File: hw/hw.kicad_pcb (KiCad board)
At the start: 2 copper layers, 120 x 50 mm, 91 parts, among them J1 USB_C_Receptacle, J10 Conn_01x04_Male, J11 Conn_01x04_Male, J12 Conn_01x04_Male, J13 Conn_01x04_Male, J14 Conn_01x04_Male, J16 Conn_01x02_Female, J17 Conn_01x02_Female, J18 Conn_01x04_Female, J19 Conn_01x08_Male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

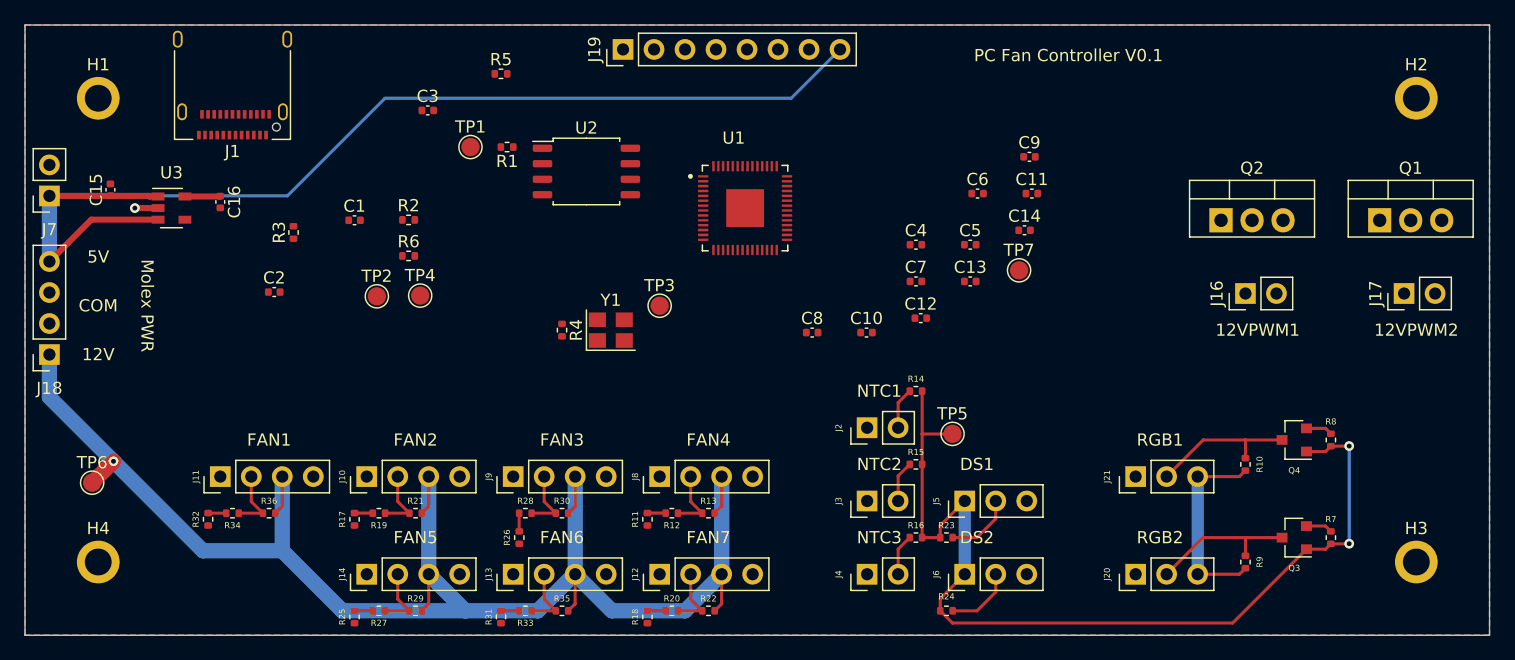
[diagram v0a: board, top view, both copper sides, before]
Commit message: rooting progress + update readme + change power transistor
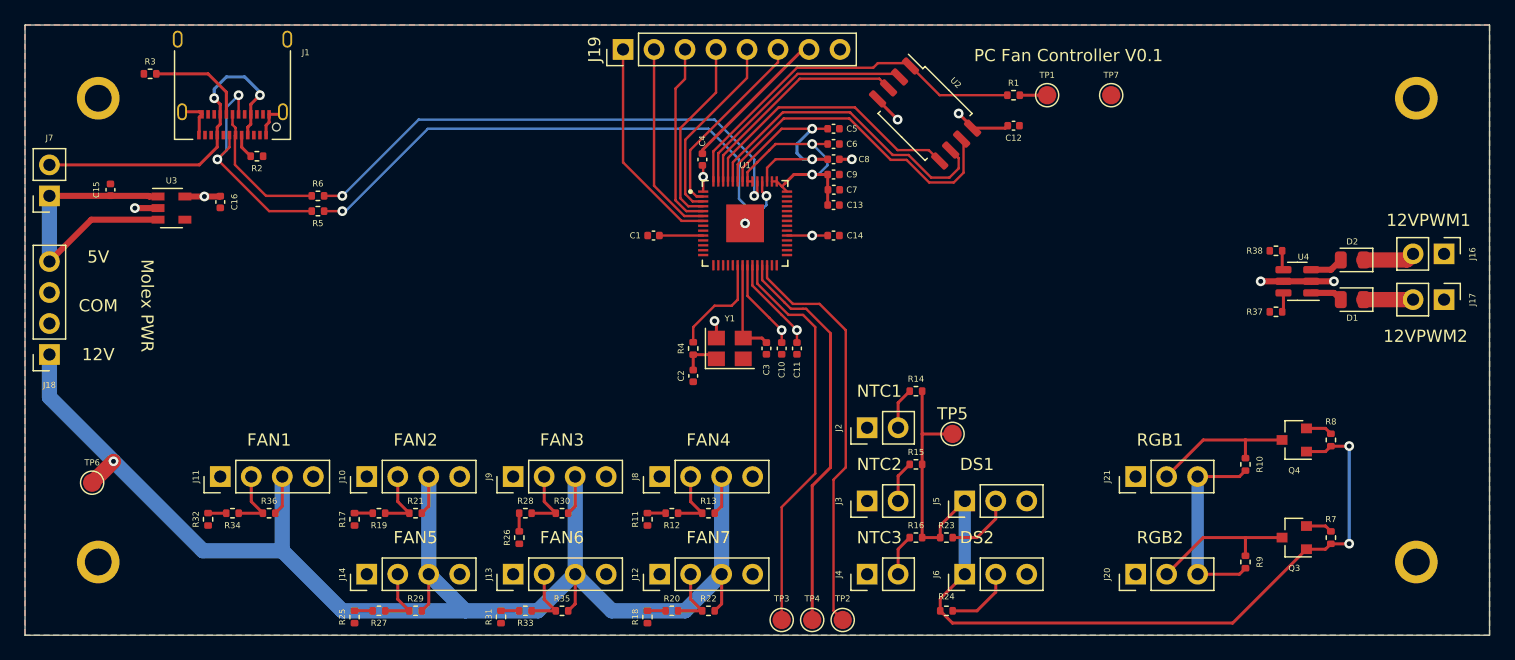
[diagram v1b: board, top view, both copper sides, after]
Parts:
- removed Q1, Q2: IRF540N, Package_TO_SOT_THT:TO-220-3_Vertical
- added D1: D, Diode_SMD:D_0805_2012Metric, F.Cu at (188.8, 42.5)
- added D2: D, Diode_SMD:D_0805_2012Metric, F.Cu at (188.8, 39.2)
- added R37: 10K, Resistor_SMD:R_0402_1005Metric, F.Cu at (182.5, 43.5)
- added R38: 10K, Resistor_SMD:R_0402_1005Metric, F.Cu at (182.5, 38.5)
- added U4: TPM8205ATS6, Package_TO_SOT_SMD:TSOT-23-6, F.Cu at (184.2, 41.0)
- moved TP1 47.4 mm to (163.8, 25.8)
- moved TP2 46.5 mm to (147.0, 68.8), turned to 180 degrees
- moved R1 41.7 mm to (161.0, 25.8), turned to 0 degrees
- moved TP4 41.7 mm to (144.5, 68.8), turned to 180 degrees
- moved C2 35.0 mm to (134.8, 48.8), turned to -90 degrees
- moved C3 33.9 mm to (140.8, 46.5), turned to -90 degrees
- moved U2 28.2 mm to (153.8, 27.2), turned to -45 degrees
- moved TP3 27.6 mm to (142.0, 68.8), turned to 180 degrees
- moved C1 24.5 mm to (131.5, 37.2), turned to 180 degrees
- moved C11 23.1 mm to (143.2, 46.5), turned to -90 degrees
- moved C4 18.8 mm to (135.5, 31.0), turned to 90 degrees
- moved R5 18.8 mm to (104.0, 35.2)
- moved R3 17.5 mm to (90.2, 24.0), turned to 0 degrees
- moved C12 17.5 mm to (161.0, 28.2)
- moved J16 16.6 mm to (196.3, 38.8), turned to -90 degrees
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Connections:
- C3 pad 1: /XI -> /XO
- J1 pad A10: Net-(J1-PadA10) -> unconnected-(J1-PadA10)
- J1 pad A11: Net-(J1-PadA11) -> unconnected-(J1-PadA11)
- J1 pad A2: Net-(J1-PadA2) -> unconnected-(J1-PadA2)
- J1 pad A3: Net-(J1-PadA3) -> unconnected-(J1-PadA3)
- J1 pad A8: Net-(J1-PadA8) -> unconnected-(J1-PadA8)
- J1 pad B10: Net-(J1-PadB10) -> unconnected-(J1-PadB10)
- J1 pad B11: Net-(J1-PadB11) -> unconnected-(J1-PadB11)
- J1 pad B2: Net-(J1-PadB2) -> unconnected-(J1-PadB2)
- J1 pad B3: Net-(J1-PadB3) -> unconnected-(J1-PadB3)
- J1 pad B8: Net-(J1-PadB8) -> unconnected-(J1-PadB8)
- J16 pad 1: Net-(J16-Pad1) -> GND
- J17 pad 1: Net-(J17-Pad1) -> GND
- J19 pad 8: +5V -> +3.3V
- R4 pad 1: /XO -> /XI
- U1 pad 41: Net-(U1-Pad41) -> unconnected-(U1-Pad41)
- U3 pad 4: Net-(U3-Pad4) -> unconnected-(U3-Pad4)
- Y1 pad 3: /XI -> /XO
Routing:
- net +5V: track 110.6 -> 40.9 mm
- net Net-(U1-Pad46): track 0.00 -> 45.8 mm, vias 0 -> 2
- net Net-(U1-Pad47): track 0.00 -> 43.5 mm, vias 0 -> 2
- net +3V3: track 80.9 -> 122.9 mm, vias 2 -> 9
- net Net-(U1-Pad26): track 0.00 -> 33.7 mm
- net Net-(U1-Pad24): track 0.00 -> 32.9 mm
- net Net-(U1-Pad25): track 0.00 -> 32.7 mm
- net /QSPI_SS: track 0.00 -> 30.6 mm
- net Net-(J1-PadA4): track 0.00 -> 28.0 mm, vias 0 -> 2
- net +1V1: track 0.00 -> 27.6 mm, vias 0 -> 3
- net /QSPI_SD3: track 0.00 -> 26.8 mm
- net /QSPI_SCLK: track 0.00 -> 26.1 mm
- net GND: track 1.90 -> 25.5 mm, vias 1 -> 5
- net /QSPI_SD0: track 0.00 -> 22.8 mm
- net /QSPI_SD1: track 0.00 -> 20.0 mm
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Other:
- net class Default removed

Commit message: wip
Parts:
- moved C14 3.75 mm to (150.0, 37.2)
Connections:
- U1 pad 11: /PWM3 -> /PWM7
- U1 pad 12: /PWM4 -> /tach5
- U1 pad 13: /PWM5 -> /PWM8
- U1 pad 14: /PWM6 -> /tach6
- U1 pad 15: /PWM7 -> /PWM5
- U1 pad 16: /PWM8 -> /tach3
- U1 pad 17: /PWM9 -> /PWM6
- U1 pad 18: /tach1 -> /tach4
- U1 pad 27: /tach2 -> /PWM3
- U1 pad 28: /tach3 -> /tach1
- U1 pad 29: /tach4 -> /PWM4
- U1 pad 30: /tach5 -> /tach2
- U1 pad 31: /tach6 -> /PWM1
- U1 pad 32: /tach7 -> /PWM2
- U1 pad 8: /PWM1 -> /PWM9
- U1 pad 9: /PWM2 -> /tach7
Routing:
- net /RGB1: track 2.18 -> 63.8 mm, vias 0 -> 2
- net /RGB2: track 2.18 -> 55.2 mm, vias 0 -> 2
- net /PWM9: track 0.00 -> 50.5 mm
- net /tach7: track 5.37 -> 54.0 mm
- net /DS2: track 5.63 -> 53.3 mm, vias 0 -> 2
- net /PWM1: track 1.59 -> 43.9 mm
- net /PWM2: track 1.59 -> 43.3 mm
- net /PWM8: track 0.00 -> 41.1 mm
- net /tach2: track 5.37 -> 44.8 mm, vias 0 -> 2
- net /PWM4: track 0.00 -> 39.2 mm, vias 0 -> 2
- net /DS1: track 5.63 -> 44.3 mm, vias 0 -> 2
- net /tach6: track 5.37 -> 43.7 mm
- net /PWM7: track 0.00 -> 38.1 mm
- net /tach5: track 5.37 -> 41.1 mm
- net /PWM6: track 0.00 -> 33.6 mm
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
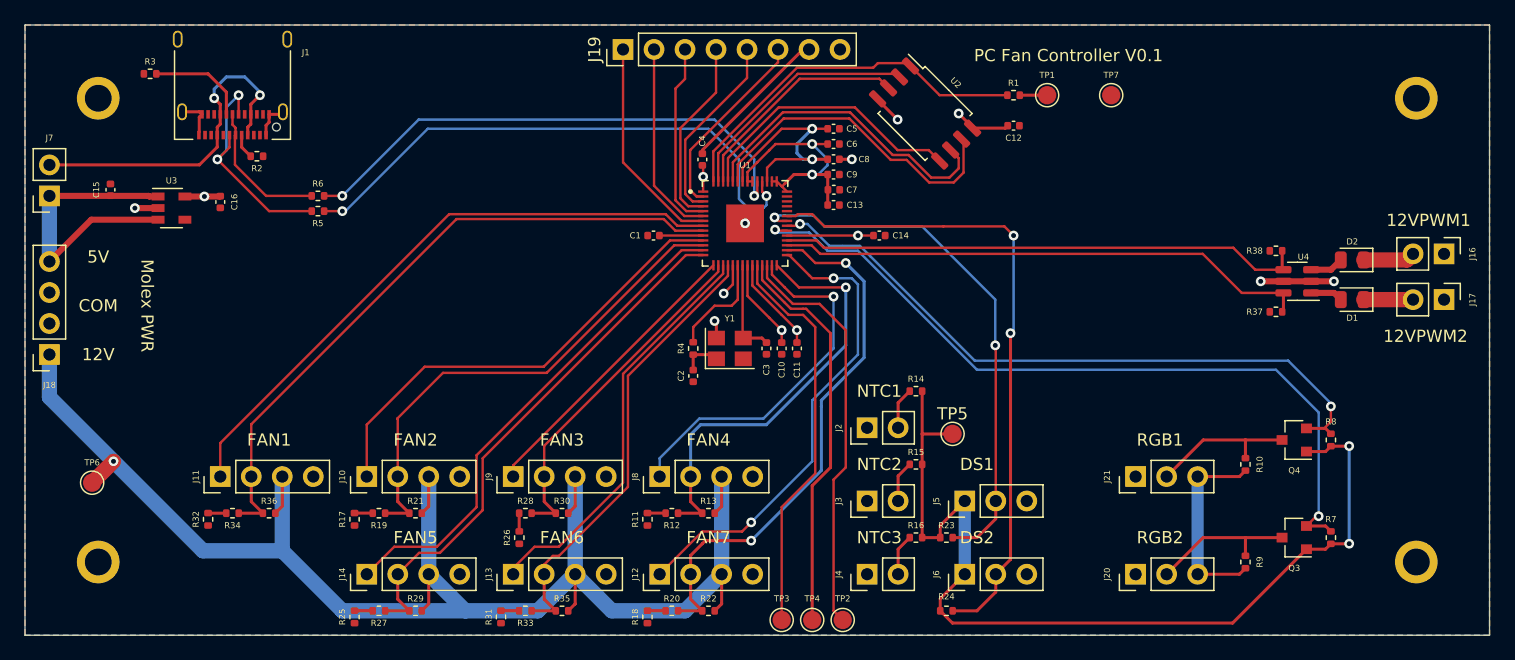
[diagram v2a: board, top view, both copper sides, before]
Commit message: add label, fix 12 v track width, connect everything
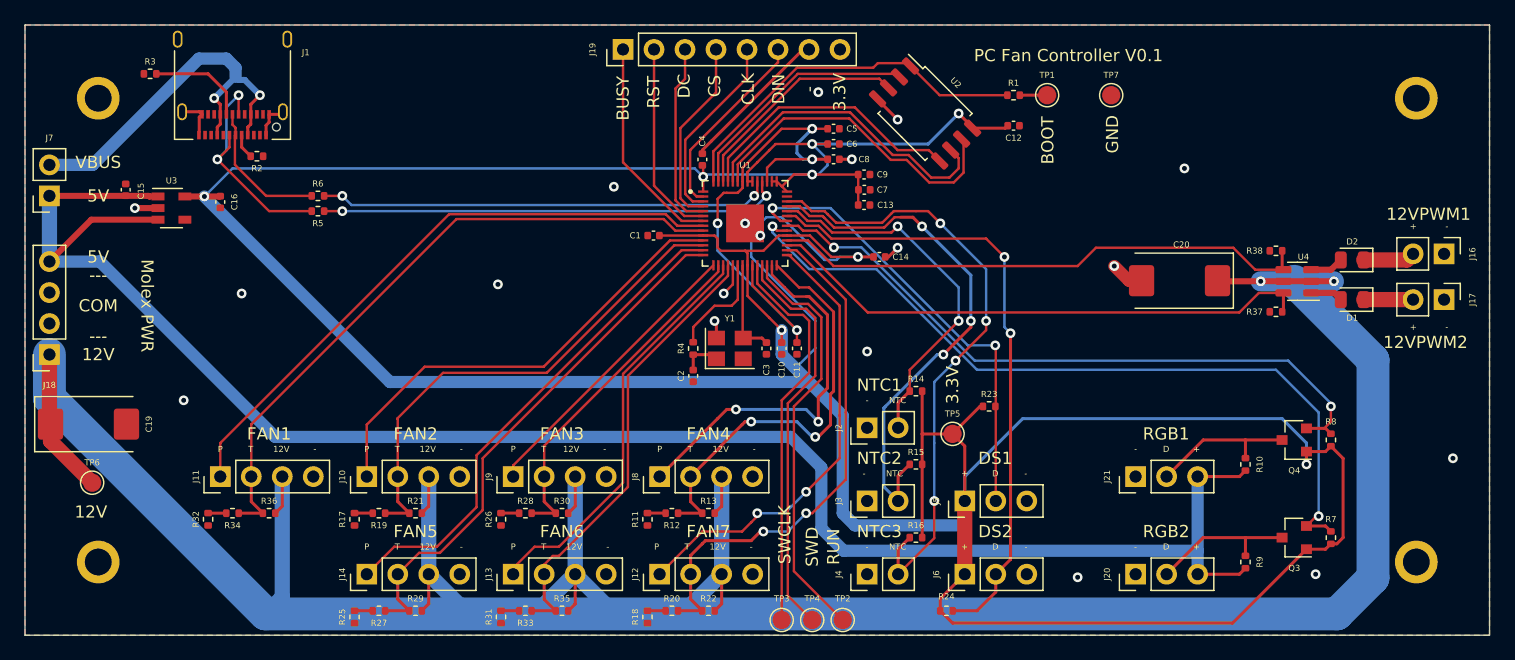
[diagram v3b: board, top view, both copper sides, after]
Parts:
- added C19: 100uF, Capacitor_Tantalum_SMD:CP_EIA-7343-43_Kemet-X, F.Cu at (85.2, 52.7)
- added C20: 100uF, Capacitor_Tantalum_SMD:CP_EIA-7343-43_Kemet-X, F.Cu at (174.6, 41.0)
- moved R23 11.3 mm to (159.0, 51.2)
- moved C13 2.50 mm to (148.8, 34.8)
- moved C7 2.50 mm to (148.8, 33.5)
- moved C9 2.50 mm to (148.8, 32.2)
- moved R26 2.12 mm to (119.0, 60.5)
- moved C14 1.75 mm to (150.0, 39.0)
- moved C15 1.25 mm to (88.2, 33.5)
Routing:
- net +3V3: track 126.6 -> 351.3 mm, vias 9 -> 8
- net +12V: track 135.0 -> 250.5 mm, vias 3 -> 2
- net +5V: track 40.9 -> 147.7 mm
- net /NTC3: track 3.39 -> 50.8 mm, vias 0 -> 4
- net /NTC2: track 3.39 -> 43.7 mm, vias 0 -> 3
- net /NTC1: track 3.39 -> 30.6 mm, vias 0 -> 2
- net +1V1: track 27.6 -> 44.0 mm, vias 3 -> 4
- net Net-(R5-Pad2): track 45.8 -> 38.1 mm
- net /DS1: track 44.3 -> 37.5 mm
- net Net-(R6-Pad2): track 43.5 -> 37.1 mm
- net GND: track 28.1 -> 32.2 mm, vias 6 -> 19
- net Net-(J1-PadA4): track 28.0 -> 32.0 mm
- net /PWM4: track 39.2 -> 37.4 mm
- net /DS2: track 53.3 -> 51.5 mm
- net /tach2: track 44.8 -> 43.4 mm
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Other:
- board text added: "+"
- board text added: "-"
- board text added: "---"
- board text added: "3.3V"
- board text added: "BOOT"
- board text added: "BUSY"
- board text added: "CLK"
- board text added: "CS"
- board text added: "D"
- board text added: "DC"
- board text added: "DIN"
- board text added: "GND"
- board text added: "NTC"
- board text added: "P"
- board text added: "RST"
- board text added: "RUN"
- board text added: "SWCLK"
- board text added: "SWD"
- board text added: "T"
- board text added: "VBUS"

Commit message: reduce size of the board and update readme
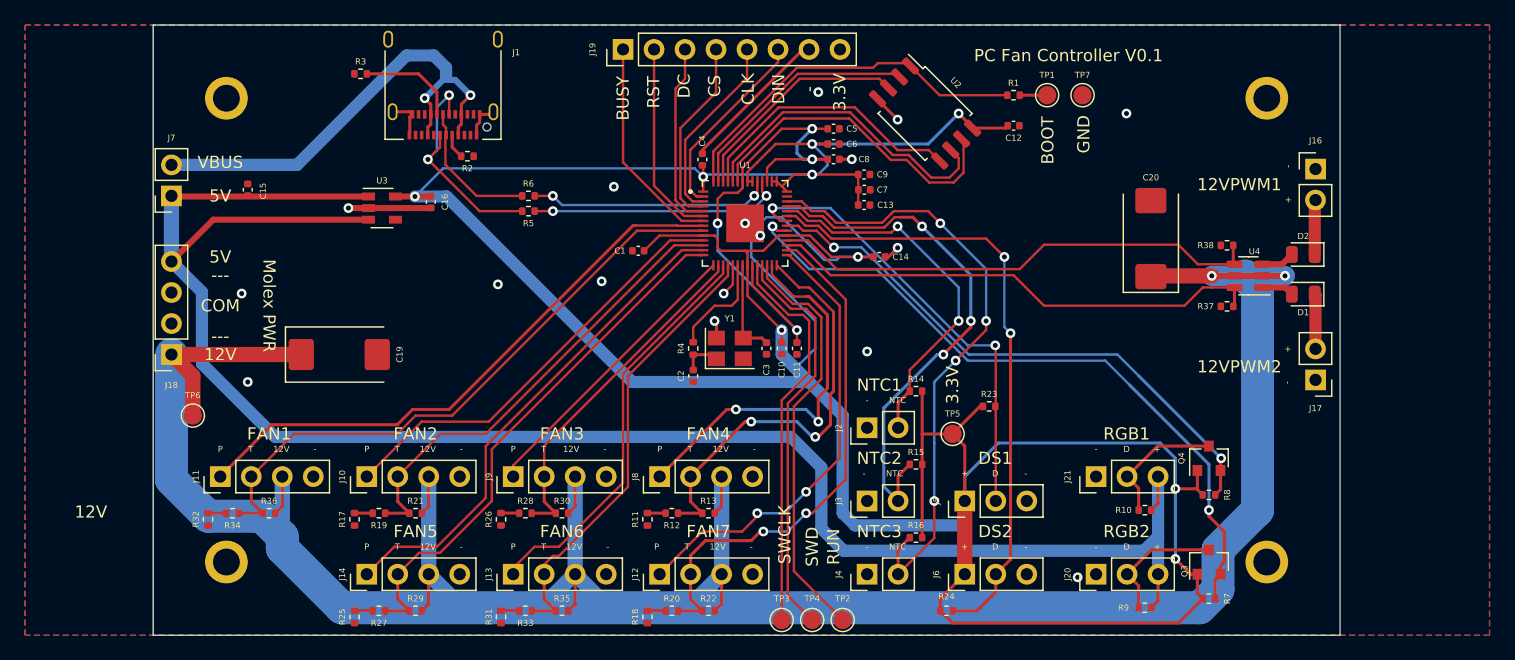
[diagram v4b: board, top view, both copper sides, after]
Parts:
- moved C19 21.3 mm to (105.8, 47.0)
- moved C16 17.2 mm to (113.2, 34.5)
- moved J1 17.2 mm to (114.2, 24.0)
- moved R2 17.2 mm to (116.2, 30.8)
- moved R3 17.2 mm to (107.5, 24.0)
- moved R5 17.2 mm to (121.2, 35.2)
- moved R6 17.2 mm to (121.2, 34.0)
- moved U3 17.2 mm to (109.2, 35.0)
- moved J16 12.6 mm to (185.7, 31.8), turned to 0 degrees
- moved J17 12.4 mm to (185.7, 49.1), turned to 180 degrees
- moved H2 12.2 mm to (181.8, 26.0)
- moved H3 12.2 mm to (181.8, 64.0)
- moved R7 11.2 mm to (177.0, 67.0), turned to 0 degrees
- moved R8 11.0 mm to (177.0, 58.5), turned to 0 degrees
- moved H1 10.5 mm to (96.5, 26.0)
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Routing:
- net +3V3: track 351.3 -> 297.0 mm, vias 8 -> 9
- net +12V: track 250.5 -> 231.0 mm
- net Net-(R6-Pad2): track 37.1 -> 19.9 mm
- net Net-(R5-Pad2): track 38.1 -> 20.8 mm
- net /RGB2: track 55.1 -> 46.7 mm
- net Net-(J1-PadA4): track 32.0 -> 39.5 mm
- net /RGB1: track 64.7 -> 57.3 mm
- net /PWM1: track 45.2 -> 40.8 mm
- net /PWM2: track 44.5 -> 40.6 mm
- net /tach7: track 54.0 -> 50.7 mm
- net +5V: track 147.7 -> 150.6 mm
- net /tach5: track 41.1 -> 38.2 mm
- net /PWM7: track 38.1 -> 35.6 mm
- net /PWM9: track 50.5 -> 48.1 mm
- net GND: track 32.2 -> 34.3 mm, vias 19 -> 17
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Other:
- board size 120 x 50 mm -> 97.2 x 50 mm

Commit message: add dht11/22 support
hwmon have humidity support and... i have some dht laying aroung ...
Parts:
- added R39: 4.7K, Resistor_SMD:R_0402_1005Metric, F.Cu at (165.0, 32.0)
- added U5: DHT11, Sensor:Aosong_DHT11_5.5x12.0_P2.54mm, F.Cu at (163.5, 35.9)
- moved C20 6.50 mm to (172.5, 44.0), turned to -90 degrees
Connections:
- U1 pad 41: unconnected-(U1-Pad41) -> /dht_data
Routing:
- net /dht_data: track 0.00 -> 30.5 mm
- net +3V3: track 297.0 -> 307.3 mm
